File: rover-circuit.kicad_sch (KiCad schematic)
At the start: 8 parts

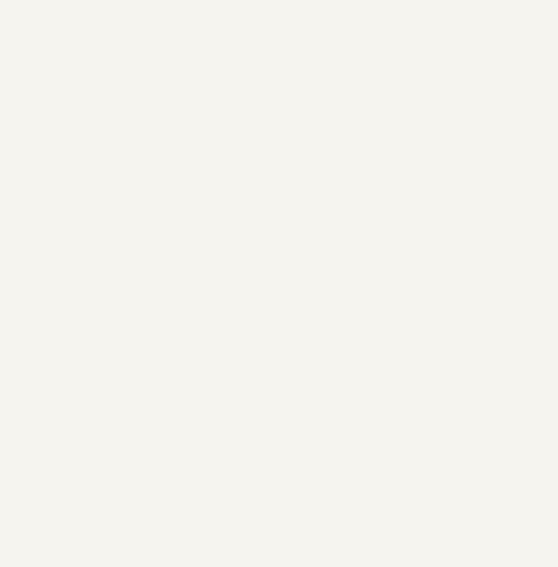
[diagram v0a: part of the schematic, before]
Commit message: add recharger module
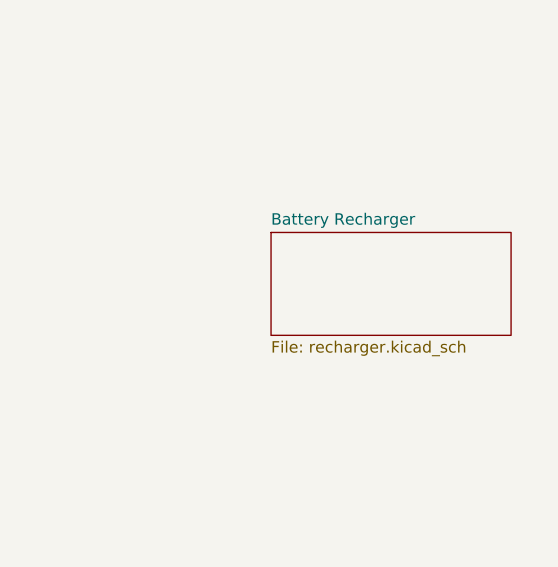
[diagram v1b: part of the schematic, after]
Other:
- added sheet Battery Recharger (recharger.kicad_sch)
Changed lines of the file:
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@@
+		)
+	)
+	(sheet
+		(at 209.55 118.11)
+		(size 26.67 11.43)
+		(exclude_from_sim no)
+		(in_bom yes)
+		(on_board yes)
+		(dnp no)
+		(fields_autoplaced yes)
+		(stroke
+			(width 0.1524)
+			(type solid)
+		)
+		(fill
+			(color 0 0 0 0.0000)
+		)
+		(property "Sheetname" "Battery Recharger"
+			(at 209.55 117.3984 0)
+			(effects
+				(font
+					(size 1.27 1.27)
+				)
+				(justify left bottom)
+			)
+		)
+		(property "Sheetfile" "recharger.kicad_sch"
+			(at 209.55 130.1246 0)
+			(effects
+				(font
+					(size 1.27 1.27)
+				)
+				(justify left top)
+			)
+		)
+		(instances
+			(project "rover-circuit"
+				(path "/0461baee-3b25-4e1a-a5c1-d76b4b99c66c"
+					(page "5")
+				)
+			)
 		)
 	)

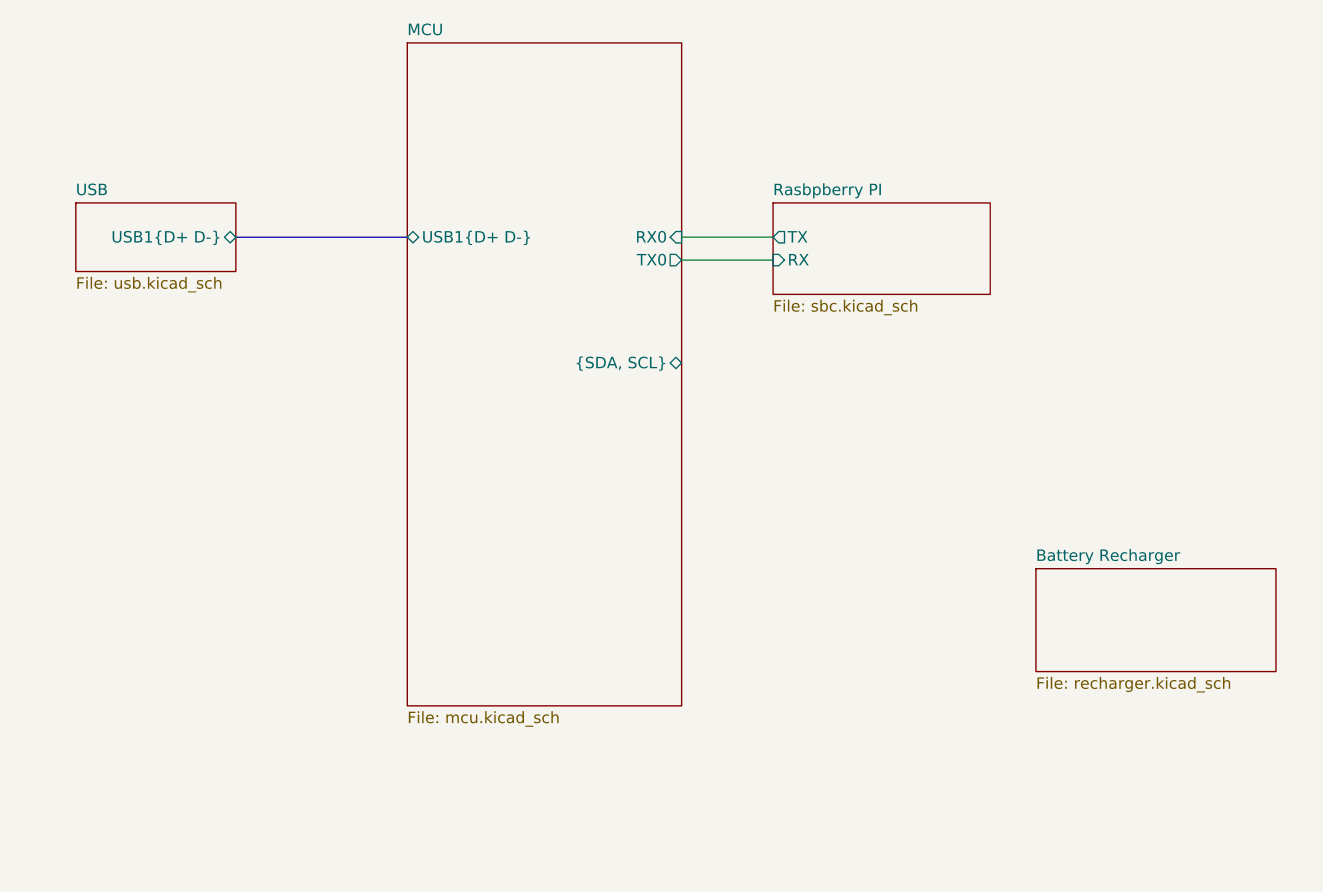
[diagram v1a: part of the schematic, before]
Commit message: update schematic
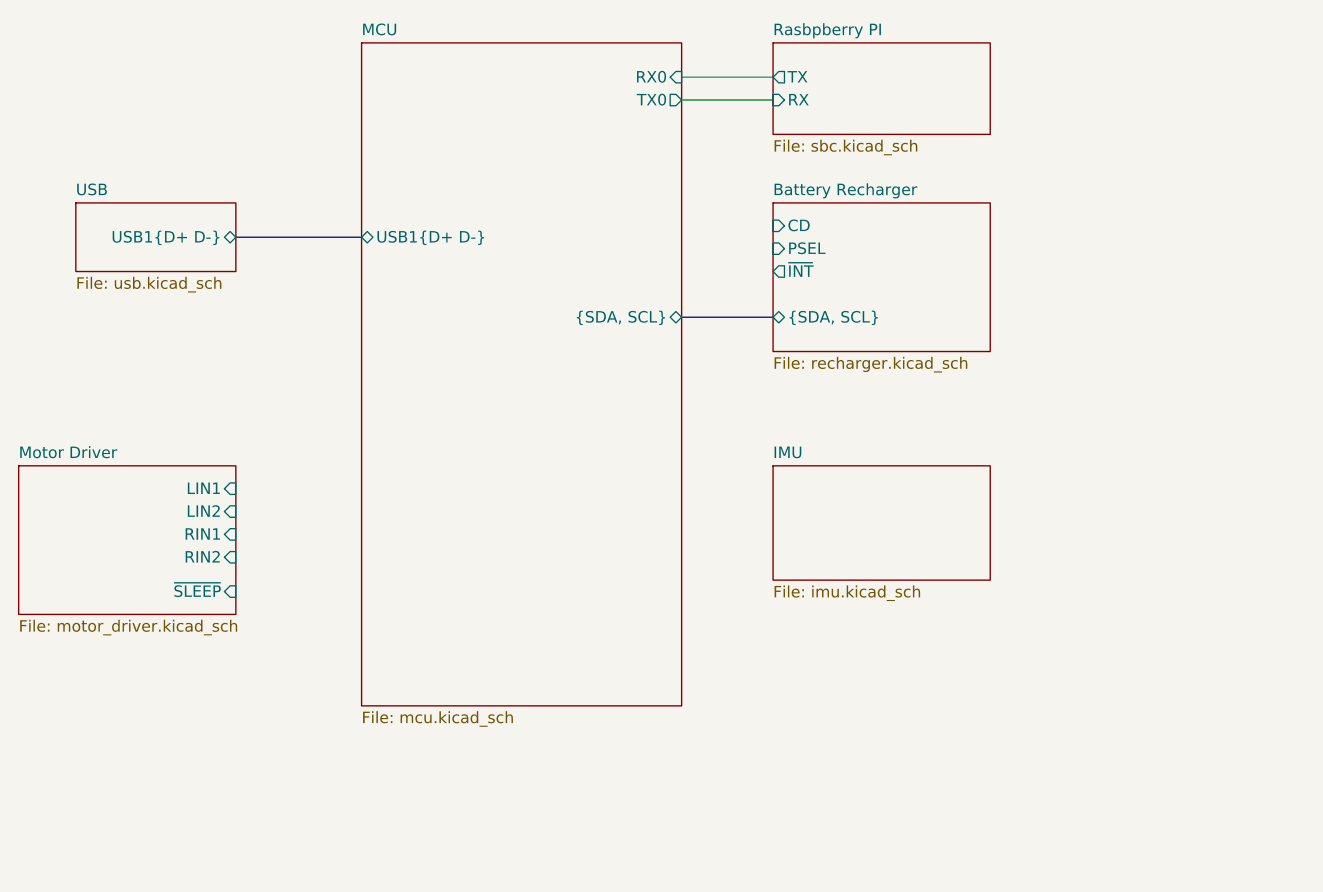
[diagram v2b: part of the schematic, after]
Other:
- added sheet IMU (imu.kicad_sch)
- added sheet Motor Driver (motor_driver.kicad_sch)
- sheet Battery Recharger ports: added CD, PSEL, {SDA, SCL}, ~{INT}; removed none

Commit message: update schematic
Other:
- sheet IMU ports: added {SDA,SCL}; removed none
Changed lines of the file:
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@@
 		(comment 4 "Nicolas Farabegoli")
+	)
+	(junction
+		(at 175.26 90.17)
+		(diameter 0)
+		(color 0 0 0 0)
 	)
 	(wire
@@
 	(bus
 		(pts
-			(xy 120.65 81.28) (xy 134.62 81.28)
+			(xy 180.34 110.49) (xy 176.53 110.49)
 		)
 		(stroke
@@
 	(bus
 		(pts
-			(xy 170.18 90.17) (xy 180.34 90.17)
+			(xy 175.26 90.17) (xy 180.34 90.17)
+		)
+		(stroke
+			(width 0)
+			(type default)
+		)
+	)
+	(bus
+		(pts
+			(xy 120.65 81.28) (xy 134.62 81.28)
+		)
+		(stroke
+			(width 0)
+			(type default)
+		)
+	)
+	(bus
+		(pts
+			(xy 170.18 90.17) (xy 175.26 90.17)
+		)
+		(stroke
+			(width 0)
+			(type default)
+		)
+	)
+	(bus
+		(pts
+			(xy 176.53 110.49) (xy 175.26 109.22)
 		)
 		(stroke
@@
 		(pts
 			(xy 170.18 63.5) (xy 180.34 63.5)
+		)
+		(stroke
+			(width 0)
+			(type default)
+		)
+	)
+	(bus
+		(pts
+			(xy 175.26 90.17) (xy 175.26 109.22)
 		)
 		(stroke
@@
 			)
 		)
+		(pin "{SDA,SCL}" bidirectional
+			(at 180.34 110.49 180)
+			(effects
+				(font
+					(size 1.27 1.27)
+				)
+				(justify left)
+			)
+		)

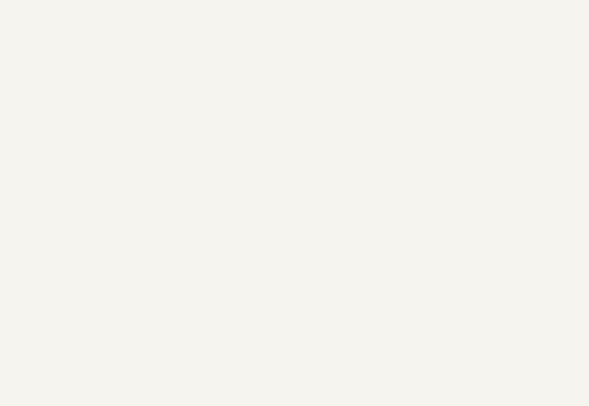
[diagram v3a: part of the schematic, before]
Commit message: update schematic
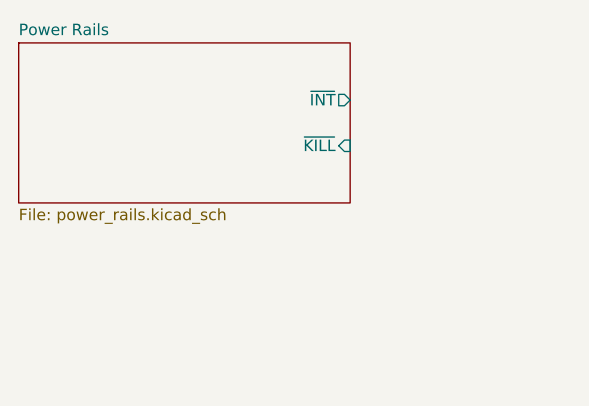
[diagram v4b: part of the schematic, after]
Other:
- added sheet Power Rails (power_rails.kicad_sch)
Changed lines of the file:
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@@
+		)
+	)
+	(sheet
+		(at 35.56 33.02)
+		(size 36.83 17.78)
+		(exclude_from_sim no)
+		(in_bom yes)
+		(on_board yes)
+		(dnp no)
+		(fields_autoplaced yes)
+		(stroke
+			(width 0.1524)
+			(type solid)
+		)
+		(fill
+			(color 0 0 0 0)
+		)
+		(property "Sheetname" "Power Rails"
+			(at 35.56 32.3084 0)
+			(show_name no)
+			(do_not_autoplace no)
+			(effects
+				(font
+					(size 1.27 1.27)
+				)
+				(justify left bottom)
+			)
+		)
+		(property "Sheetfile" "power_rails.kicad_sch"
+			(at 35.56 51.3846 0)
+			(show_name no)
+			(do_not_autoplace no)
+			(effects
+				(font
+					(size 1.27 1.27)
+				)
+				(justify left top)
+			)
+		)
+		(pin "~{INT}" output
+			(at 72.39 39.37 0)
+			(effects
+				(font
+					(size 1.27 1.27)
+				)
+				(justify right)
+			)
+		)
+		(pin "~{KILL}" input
+			(at 72.39 44.45 0)
+			(effects
+				(font
+					(size 1.27 1.27)
+				)
+				(justify right)
+			)
+		)
+		(instances
+			(project "rover-circuit"
+				(path "/0461baee-3b25-4e1a-a5c1-d76b4b99c66c"
+					(page "8")
+				)
+			)
 		)
 	)

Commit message: add uwm and refactoring
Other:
- added sheet Oled Display (display.kicad_sch)
- added sheet UWB (uwb.kicad_sch)
- sheet MCU ports: added {MISO MOSI CLK}; removed none
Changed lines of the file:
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@@
+	)
+	(junction
+		(at 175.26 105.41)
+		(diameter 0)
+		(color 0 0 0 0)
 	)
 	(junction
@@
 		(color 0 0 0 0)
 	)
+	(bus
+		(pts
+			(xy 175.26 105.41) (xy 175.26 120.65)
+		)
+		(stroke
+			(width 0)
+			(type default)
+		)
+	)
 	(wire
 		(pts
@@
 	(bus
 		(pts
-			(xy 180.34 110.49) (xy 176.53 110.49)
+			(xy 120.65 129.54) (xy 134.62 129.54)
+		)
+		(stroke
+			(width 0)
+			(type default)
+		)
+	)
+	(bus
+		(pts
+			(xy 175.26 120.65) (xy 180.34 120.65)
 		)
 		(stroke
@@
 	(bus
 		(pts
-			(xy 176.53 110.49) (xy 175.26 109.22)
+			(xy 175.26 90.17) (xy 175.26 105.41)
+		)
+		(stroke
+			(width 0)
+			(type default)
+		)
+	)
+	(bus
+		(pts
+			(xy 175.26 105.41) (xy 180.34 105.41)
 		)
 		(stroke
@@
 		(pts
 			(xy 170.18 63.5) (xy 180.34 63.5)
-		)
-		(stroke
-			(width 0)
-			(type default)
-		)
-	)
-	(bus
-		(pts
-			(xy 175.26 90.17) (xy 175.26 109.22)
 		)
 		(stroke
@@
 	)
 	(sheet
-		(at 102.87 77.47)
-		(size 17.78 7.62)
+		(at 180.34 116.84)
+		(size 24.13 7.62)
 		(exclude_from_sim no)
 		(in_bom yes)
@@
 			(color 0 0 0 0)
 		)
+		(property "Sheetname" "Oled Display"
+			(at 180.34 116.1284 0)
+			(show_name no)
+			(do_not_autoplace no)
+			(effects
+				(font
+					(size 1.27 1.27)
+				)
+				(justify left bottom)
+			)
+		)
+		(property "Sheetfile" "display.kicad_sch"
+			(at 180.34 125.0446 0)
+			(show_name no)
+			(do_not_autoplace no)
+			(effects
+				(font
+					(size 1.27 1.27)
+				)
+				(justify left top)
+			)
+		)
+		(pin "{SDA,SCL}" bidirectional
+			(at 180.34 120.65 180)
+			(effects
+				(font
+					(size 1.27 1.27)
+				)
+				(justify left)
+			)
+		)
+		(instances
+			(project "rover-circuit"
+				(path "/0461baee-3b25-4e1a-a5c1-d76b4b99c66c"
+					(page "9")
+				)
+			)
+		)
+	)
+	(sheet
+		(at 95.25 77.47)
+		(size 25.4 7.62)
+		(exclude_from_sim no)
+		(in_bom yes)
+		(on_board yes)
+		(dnp no)
+		(fields_autoplaced yes)
+		(stroke
+			(width 0.1524)
+			(type solid)
+		)
+		(fill
+			(color 0 0 0 0)
+		)
 		(property "Sheetname" "USB"
-			(at 102.87 76.7584 0)
+			(at 95.25 76.7584 0)
 			(show_name no)
 			(do_not_autoplace no)
@@
 		)
 		(property "Sheetfile" "usb.kicad_sch"
-			(at 102.87 85.6746 0)
+			(at 95.25 85.6746 0)
 			(show_name no)
 			(do_not_autoplace no)
@@
 	)
 	(sheet
-		(at 180.34 106.68)
-		(size 24.13 12.7)
+		(at 180.34 101.6)
+		(size 24.13 7.62)
 		(exclude_from_sim no)
 		(in_bom yes)
@@
 		)
 		(property "Sheetname" "IMU"
-			(at 180.34 105.9684 0)
+			(at 180.34 100.8884 0)
 			(show_name no)
 			(do_not_autoplace no)
@@
 		)
 		(property "Sheetfile" "imu.kicad_sch"
-			(at 180.34 119.9646 0)
+			(at 180.34 109.8046 0)
 			(show_name no)
 			(do_not_autoplace no)
@@
 		)
 		(pin "{SDA,SCL}" bidirectional
-			(at 180.34 110.49 180)
+			(at 180.34 105.41 180)
 			(effects
 				(font
@@
 	)
 	(sheet
-		(at 96.52 106.68)
-		(size 24.13 16.51)
+		(at 95.25 92.71)
+		(size 25.4 16.51)
 		(exclude_from_sim no)
 		(in_bom yes)
@@
 		)
 		(property "Sheetname" "Motor Driver"
-			(at 96.52 105.9684 0)
+			(at 95.25 91.9984 0)
 			(show_name no)
 			(do_not_autoplace no)
@@
 		)
 		(property "Sheetfile" "motor_driver.kicad_sch"
-			(at 96.52 123.7746 0)
+			(at 95.25 109.8046 0)
 			(show_name no)
 			(do_not_autoplace no)
@@
 		)
 		(pin "LIN1" input
-			(at 120.65 109.22 0)
+			(at 120.65 95.25 0)
 			(effects
 				(font
@@
 		)
 		(pin "LIN2" input
-			(at 120.65 111.76 0)
+			(at 120.65 97.79 0)
 			(effects
 				(font
@@
 		)
 		(pin "RIN1" input
-			(at 120.65 114.3 0)
+			(at 120.65 100.33 0)
 			(effects
 				(font
@@
 		)
 		(pin "RIN2" input
-			(at 120.65 116.84 0)
+			(at 120.65 102.87 0)
 			(effects
 				(font
@@
 		)
 		(pin "~{SLEEP}" input
-			(at 120.65 120.65 0)
+			(at 120.65 106.68 0)
 			(effects
 				(font
@@
 			)
 		)
+		(pin "{MISO MOSI CLK}" bidirectional
+			(at 134.62 129.54 180)
+			(effects
+				(font
+					(size 1.27 1.27)
+				)
+				(justify left)
+			)
+		)
 		(instances
 			(project "rover-circuit"
@@
 	)
 	(sheet
-		(at 35.56 33.02)
-		(size 36.83 17.78)
+		(at 95.25 115.57)
+		(size 25.4 17.78)
 		(exclude_from_sim no)
 		(in_bom yes)
@@
 			(color 0 0 0 0)
 		)
+		(property "Sheetname" "UWB"
+			(at 95.25 114.8584 0)
+			(show_name no)
+			(do_not_autoplace no)
+			(effects
+				(font
+					(size 1.27 1.27)
+				)
+				(justify left bottom)
+			)
+		)
+		(property "Sheetfile" "uwb.kicad_sch"
+			(at 95.25 133.9346 0)
+			(show_name no)
+			(do_not_autoplace no)
+			(effects
+				(font
+					(size 1.27 1.27)
+				)
+				(justify left top)
+			)
+		)
+		(pin "UWB_IRQ" output
+			(at 120.65 119.38 0)
+			(effects
+				(font
+					(size 1.27 1.27)
+				)
+				(justify right)
+			)
+		)
+		(pin "UWB_RST" input
+			(at 120.65 121.92 0)
+			(effects
+				(font
+					(size 1.27 1.27)
+				)
+				(justify right)
+			)
+		)
+		(pin "UWB_WAKEUP" input
+			(at 120.65 124.46 0)
+			(effects
+				(font
+					(size 1.27 1.27)
+				)
+				(justify right)
+			)
+		)
+		(pin "UWB_~{CS}" input
+			(at 120.65 127 0)
+			(effects
+				(font
+					(size 1.27 1.27)
+				)
+				(justify right)
+			)
+		)
+		(pin "{MISO MOSI CLK}" bidirectional
+			(at 120.65 129.54 0)
+			(effects
+				(font
+					(size 1.27 1.27)
+				)
+				(justify right)
+			)
+		)
+		(instances
+			(project "rover-circuit"
+				(path "/0461baee-3b25-4e1a-a5c1-d76b4b99c66c"
+					(page "10")
+				)
+			)
+		)
+	)
+	(sheet
+		(at 95.25 59.69)
+		(size 25.4 11.43)
+		(exclude_from_sim no)
+		(in_bom yes)
+		(on_board yes)
+		(dnp no)
+		(fields_autoplaced yes)
+		(stroke
+			(width 0.1524)
+			(type solid)
+		)
+		(fill
+			(color 0 0 0 0)
+		)
 		(property "Sheetname" "Power Rails"
-			(at 35.56 32.3084 0)
+			(at 95.25 58.9784 0)
 			(show_name no)
 			(do_not_autoplace no)
@@
 		)
 		(property "Sheetfile" "power_rails.kicad_sch"
-			(at 35.56 51.3846 0)
+			(at 95.25 71.7046 0)
 			(show_name no)
 			(do_not_autoplace no)
@@
 		)
 		(pin "~{INT}" output
-			(at 72.39 39.37 0)
+			(at 120.65 63.5 0)
 			(effects
 				(font
@@
 		)
 		(pin "~{KILL}" input
-			(at 72.39 44.45 0)
-			(effects
-				(font
+			(at 120.65 67.31 0)
+			(effects
+				(font

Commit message: improve design
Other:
- sheet Motor Driver ports: added AIN1, AIN2, BIN1, BIN2; removed LIN1, LIN2, RIN1, RIN2
- title: Project Venice -> Dropbot
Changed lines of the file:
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@@
 	(paper "A4")
 	(title_block
-		(title "Project Venice")
+		(title "Dropbot")
 		(date "2025-06-15")
 		(company "PSLab - Università di Bologna")
@@
 			)
 		)
-		(pin "LIN1" input
-			(at 120.65 95.25 0)
-			(effects
-				(font
-					(size 1.27 1.27)
-				)
-				(justify right)
-			)
-		)
-		(pin "LIN2" input
-			(at 120.65 97.79 0)
-			(effects
-				(font
-					(size 1.27 1.27)
-				)
-				(justify right)
-			)
-		)
-		(pin "RIN1" input
-			(at 120.65 100.33 0)
-			(effects
-				(font
-					(size 1.27 1.27)
-				)
-				(justify right)
-			)
-		)
-		(pin "RIN2" input
-			(at 120.65 102.87 0)
-			(effects
-				(font
-					(size 1.27 1.27)
-				)
-				(justify right)
-			)
-		)
 		(pin "~{SLEEP}" input
 			(at 120.65 106.68 0)
 			(effects
 				(font
+					(size 1.27 1.27)
+				)
+				(justify right)
+			)
+		)
+		(pin "AIN1" input
+			(at 120.65 95.25 0)
+			(effects
+				(font
+					(size 1.27 1.27)
+				)
+				(justify right)
+			)
+		)
+		(pin "AIN2" input
+			(at 120.65 97.79 0)
+			(effects
+				(font
+					(size 1.27 1.27)
+				)
+				(justify right)
+			)
+		)
+		(pin "BIN2" input
+			(at 120.65 100.33 0)
+			(effects
+				(font
+					(size 1.27 1.27)
+				)
+				(justify right)
+			)
+		)
+		(pin "BIN1" input
+			(at 120.65 102.87 0)
+			(effects
+				(font

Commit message: moving on routing
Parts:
- removed H3, H4: MountingHole, MountingHole:MountingHole_3.2mm_M3_Pad, symbol Mechanical:MountingHole
- removed H5, H6: MountingHole, MountingHole:MountingHole_2.5mm, symbol Mechanical:MountingHole
